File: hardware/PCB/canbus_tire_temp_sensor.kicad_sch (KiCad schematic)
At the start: 45 parts, among them J2 TC2030, J3 Conn_01x06_Male, SW1 SW_Push, SW2 SW_DPDT_x2, U1 NCV8114ASN330T1G, U2 STM32G473CB, U3 TCAN3403DRQ1, Y1 16 MHz

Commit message: Initial Schematic
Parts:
- removed C11: 0.1uF, Capacitor_SMD:C_0603_1608Metric, symbol Device:C_Small
- removed C12, C13: 1uF, Capacitor_SMD:C_0603_1608Metric, symbol Device:C_Small
- removed C16: 4.7nF, Capacitor_SMD:C_0603_1608Metric, symbol Device:C_Small
- removed D4: LED, LED_SMD:LED_0603_1608Metric, symbol Device:LED
- removed H1, H2, H3, H4: MountingHole_Pad, MountingHole:MountingHole_3.2mm_M3_ISO7380_Pad_TopBottom, symbol Mechanical:MountingHole_Pad
- removed J3: Conn_01x06_Male, Connector_Molex:Molex_Micro-Fit_3.0_43650-0610_1x06-1MP_P3.00mm_Horizontal, symbol Connector:Conn_01x06_Male
- removed JP2: SolderJumper_2_Bridged, Jumper:SolderJumper-2_P1.3mm_Bridged2Bar_Pad1.0x1.5mm, symbol Jumper:SolderJumper_2_Bridged
- removed R1: 10k, Resistor_SMD:R_0603_1608Metric, symbol Device:R
- removed R10: 1k, Resistor_SMD:R_0603_1608Metric, symbol Device:R
- removed R12: 60 250mW, Resistor_SMD:R_0805_2012Metric, symbol Device:R
- removed R13: 60 250 mW, Resistor_SMD:R_0805_2012Metric, symbol Device:R
- removed R6: 22, Resistor_SMD:R_0603_1608Metric, symbol Device:R
- removed SW2: SW_DPDT_x2, Button_Switch_SMD:SW_DPDT_CK_JS202011JCQN, symbol Switch:SW_DPDT_x2
- removed U1: NCV8114ASN330T1G, Package_TO_SOT_SMD:TSOT-23-5, symbol Regulator_Linear:NCV8114ASN330T1G
- removed U2: STM32G473CB, Package_QFP:LQFP-48_7x7mm_P0.5mm, symbol MCU_ST_STM32G4:STM32G473CB
- added C?: 1uF, Capacitor_SMD:C_0603_1608Metric, symbol Device:C_Small
- added C? (x2): (no value), Capacitor_SMD:C_0603_1608Metric, symbol Device:C_Small
- added C?: 0.1uF, Capacitor_SMD:C_0603_1608Metric, symbol Device:C_Small
- added D?: (no value), symbol Device:D_TVS
- added J?: (no value), symbol Connector_Generic:Conn_01x04
- added R?: (no value), symbol Device:R_Small
- added R?: 4.7k, symbol Device:R_Small
- added TP? (x6): (no value), symbol Connector:TestPoint
- added U?: (no value), symbol canbus_tire_temp_sensor:TLE42744DV33ATMA1
- added U?: (no value), symbol MCU_ST_STM32F0:STM32F042K6Ux
- added U?: (no value), symbol canbus_tire_temp_sensor:MLX90641
- C1: value 10uF -> (none)
- C10, C9: value 0.1uF -> (none)
- C3, C4: value 1uF -> (none)
- C6, C8: value 16pF -> (none)
- Y1: value 16 MHz -> (none)
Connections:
- net +3V3: now also J2.1 (Pin_1), C?.1, C?.2, R?.1, R?.1, TP?.1, U?.1 (VDD), U?.17 (VDDIO2), U?.2 (VDD), U?.3 (Q), U?.5 (VDDA)
- net BOOT0: now also JP1.2 (C), U?.31 (PF11)
- net CANH: now also J?.3 (Pin_3)
- net CANL: now also J?.4 (Pin_4)
- net GND: now also C6.1, C?.1, C?.1, C?.1, C?.2, D?.2 (A2), J?.2 (Pin_2), TP?.1, U?.2 (GND), U?.3 (GND), U?.33 (VSS); no longer C6.2
- net NRST: now also U?.4 (NRST)
- net OSC_IN: now also C6.2, U?.2 (PF0); no longer C6.1
- net OSC_OUT: now also U?.3 (PF1)
- net SWCLK: now also U?.24 (PA14)
- net SWDIO: now also U?.23 (PA13)
- net CAN2_RX renamed CAN_RX
- net CAN_RX: now also TP?.1, U?.21 (PA11)
- net CAN2_STANDBY renamed CAN_STANDBY
- net CAN_STANDBY: now also U?.18 (PA8)
- net CAN2_TX renamed CAN_TX
- net CAN_TX: now also TP?.1, U?.22 (PA12)
- new net LED_STATUS_1: U?.26 (PB3)
- new net LED_STATUS_2: U?.25 (PA15)
- new net SCL: R?.2, TP?.1, U?.19 (PA9), U?.4 (SCL)
- new net SDA: R?.2, TP?.1, U?.1 (SDA), U?.20 (PA10)
- new net VCC: C?.2, C?.2, D?.1 (A1), J?.1 (Pin_1), U?.1 (I)
- no-connect marks 25 -> 0
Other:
- note added: "3.3V Regulator 400mA max, 4.5-40V input - reverse-polarity protection - over temperature protection - over current protection - short circuit protection"
- note added: "Hardware Requirements - MLX90641ESF-BCA-000-SP IR Sensor Array - I2C bus interface - non-isolated can transciever - robust, unable to break device easilly from power / CAN pins - must be powered from 5 - 12V, survive high transients"
- note added: "Molex-Microfit 3.0 Mating Plug: 0430250400 Mating Plug Terminals: 0430300001"
- note removed: "3.3V Regulator 300mA max"
- note removed: "External Bus Protection"
- note removed: "Hardware Requirements - MLX90641ESF-BCA-000-SP IR Sensor Array - I2C bus interface - non-isolated can transciever - selectable termination within device - robust, unable to break device easilly from power / CAN pins - must be powered from 12V vehicle battery"
- note removed: "Molex Micro-Fit with Pass-through"
- moved on the sheet: C14, C15, C6, C8, D1, D3, D7, D8, R11, R7, R9, U3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

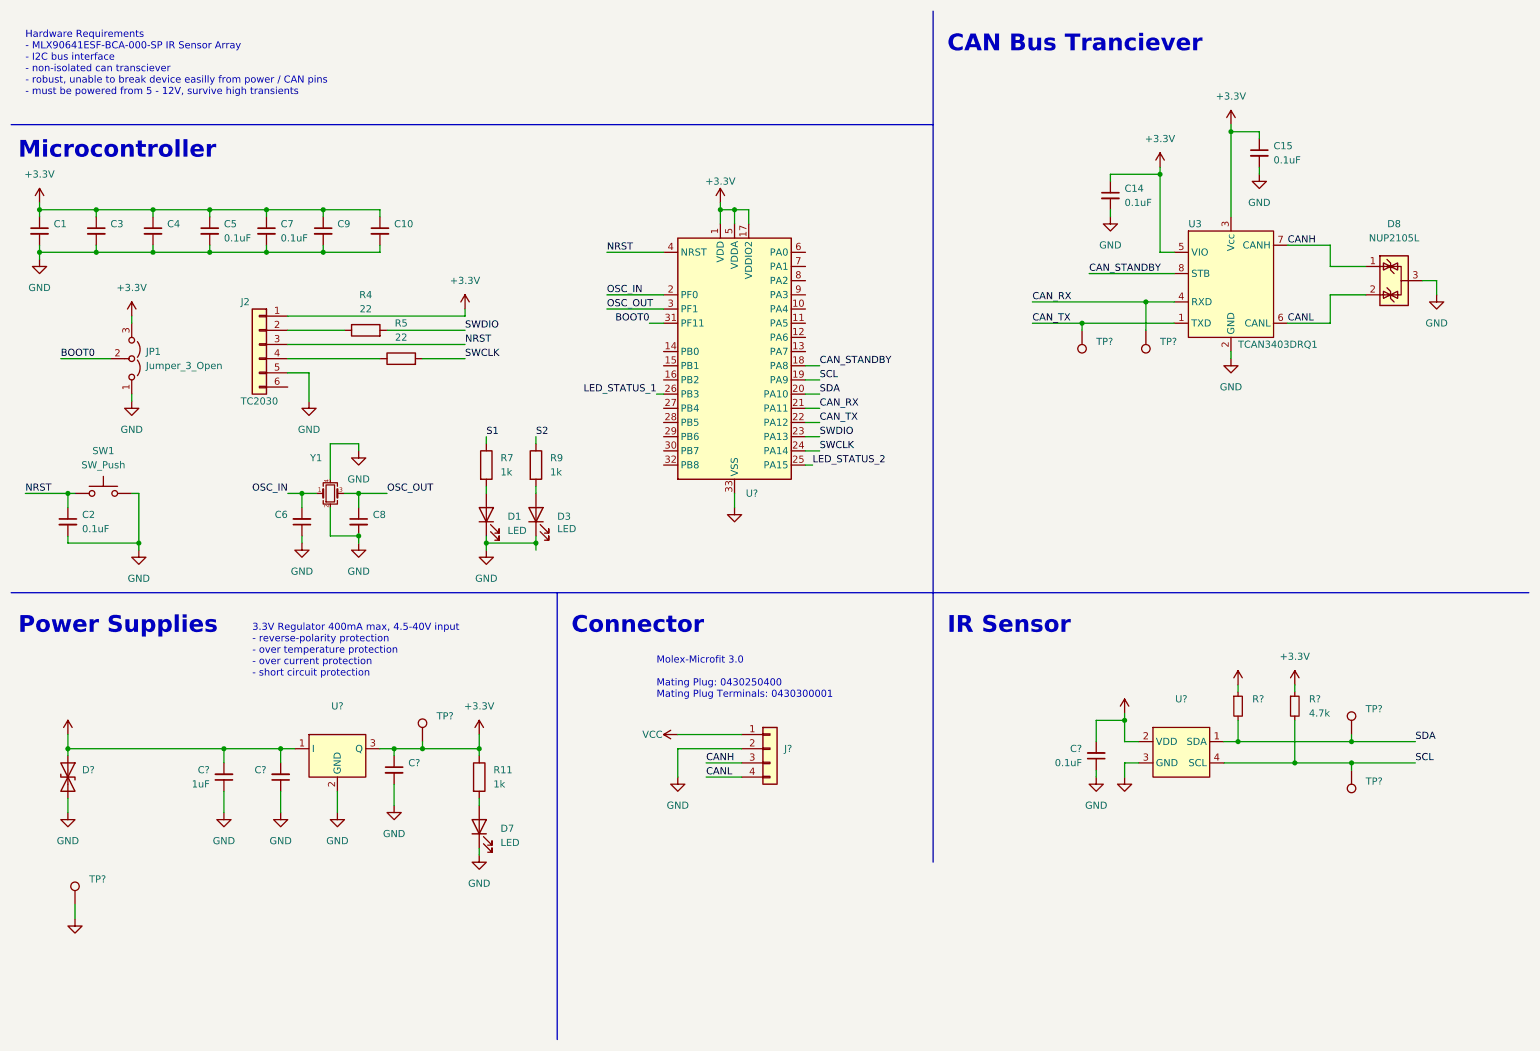
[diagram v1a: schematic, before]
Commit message: Updated footprints and ref designators
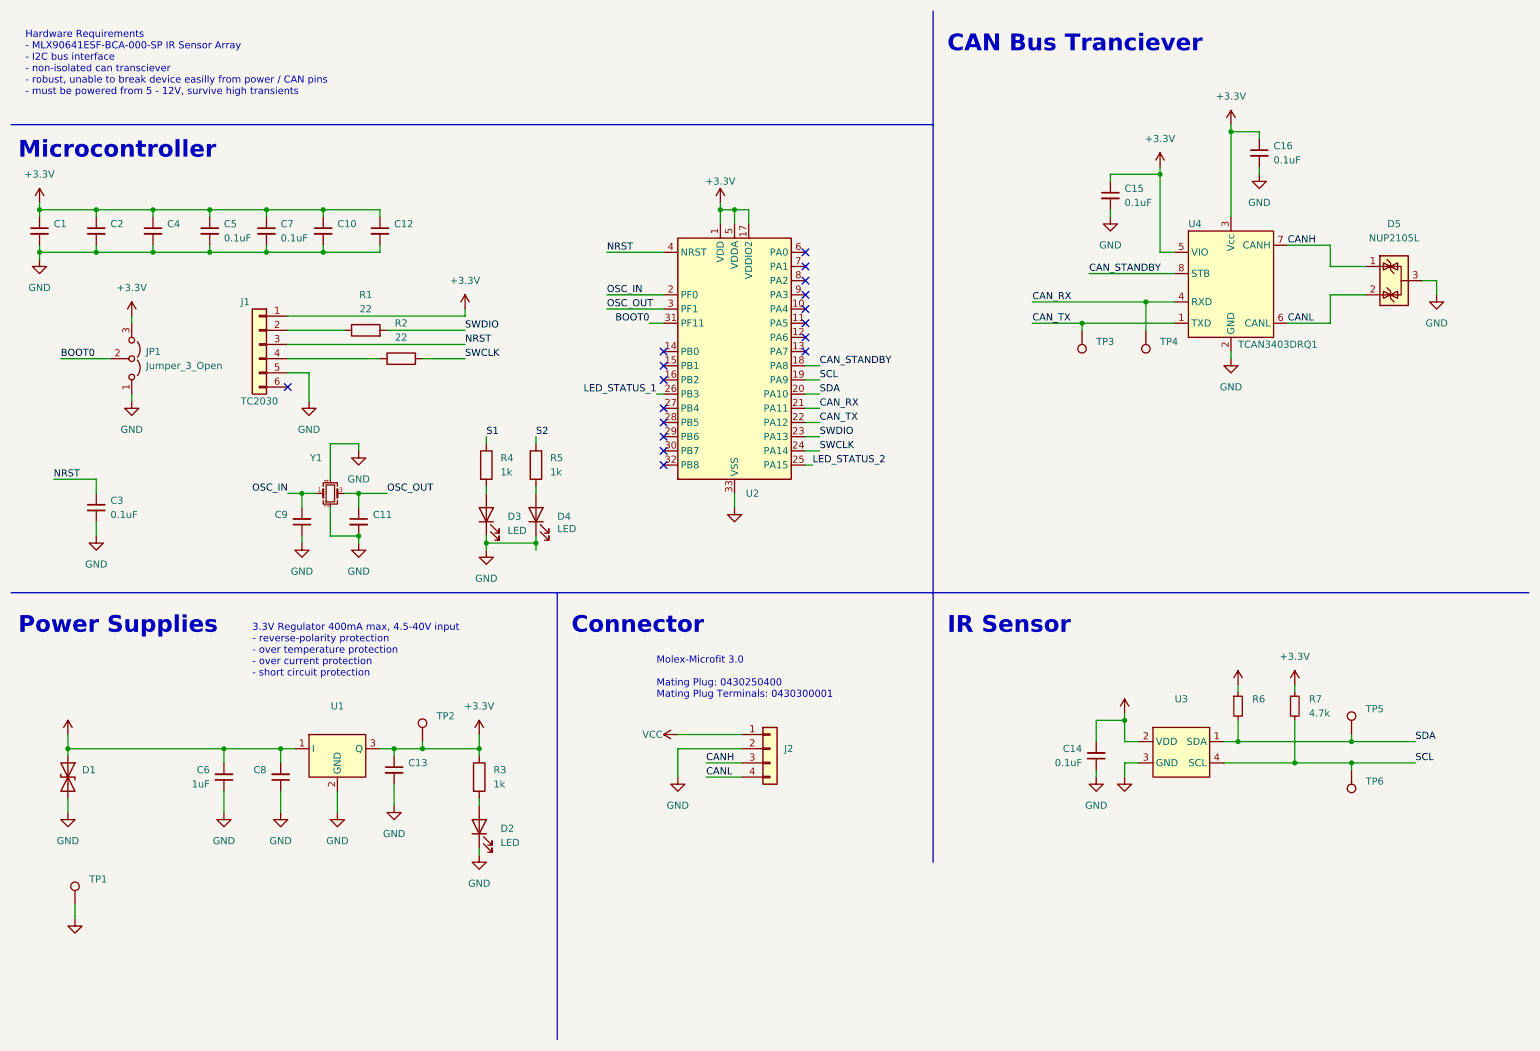
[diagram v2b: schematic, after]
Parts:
- removed SW1: SW_Push, Button_Switch_SMD:SW_SPST_B3U-1100P, symbol Switch:SW_Push
- C1: footprint Capacitor_SMD:C_0805_2012Metric -> (none)
- C13: renamed from C?; footprint Capacitor_SMD:C_0603_1608Metric -> (none)
- JP1: footprint Connector_PinHeader_2.54mm:PinHeader_1x03_P2.54mm_Vertical -> (none)
- gave numbers to parts that had none: 16
- renumbered C9 to C10, C8 to C11, C10 to C12, C14 to C15, C15 to C16, C3 to C2, C2 to C3, C6 to C9, D7 to D2, D1 to D3, D3 to D4, D8 to D5, J2 to J1, R4 to R1, R5 to R2, R11 to R3, R7 to R4, R9 to R5, U3 to U4
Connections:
- no-connect marks 0 -> 17
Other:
- moved on the sheet: C3

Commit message: initial component placement
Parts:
- J1: footprint Connector:Tag-Connect_TC2030-IDC-FP_2x03_P1.27mm_Vertical -> (none)
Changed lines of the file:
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@@
     (property "Reference" "J1" (id 0) (at 54.61 64.77 0))
     (property "Value" "TC2030" (id 1) (at 57.15 82.55 0))
-    (property "Footprint" "Connector:Tag-Connect_TC2030-IDC-FP_2x03_P1.27mm_Vertical" (id 2) (at 57.15 72.39 0)
+    (property "Footprint" "" (id 2) (at 57.15 72.39 0)
       (effects (font (size 1.27 1.27)) hide)
     )
@@
     )
     (path "/e1695a73-b49f-4d61-a6b4-7f4c0deb5b95"
-      (reference "J1") (unit 1) (value "TC2030") (footprint "Connector:Tag-Connect_TC2030-IDC-FP_2x03_P1.27mm_Vertical")
+      (reference "J1") (unit 1) (value "TC2030") (footprint "Connector:Tag-Connect_TC2030-IDC-NL_2x03_P1.27mm_Vertical")
     )
     (path "/e50c8539-9931-4edc-af04-1179e90eaec9"

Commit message: Initial board layout
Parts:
- C1: value (none) -> 4.7uF; footprint (none) -> Capacitor_SMD:C_0603_1608Metric
- C10: value (none) -> 10nF
- C11, C9: value (none) -> 12pF
- C12: value (none) -> 1uF
- C13: value (none) -> 22uF; footprint (none) -> Capacitor_SMD:C_0805_2012Metric
- C2: value (none) -> 4.7uF
- C4, C8: value (none) -> 0.1uF
- D1: value (none) -> SMBJ36CA-13-F; footprint (none) -> Diode_SMD:D_SMB
- J1: footprint (none) -> Connector:Tag-Connect_TC2030-IDC-NL_2x03_P1.27mm_Vertical
- J2: value (none) -> 0430450423; footprint (none) -> Connector_Molex:Molex_Micro-Fit_3.0_43045-0421_2x02-1MP_P3.00mm_Horizontal
- JP1: footprint (none) -> Jumper:SolderJumper-3_P1.3mm_Open_RoundedPad1.0x1.5mm
- R6: value (none) -> 4.7k; footprint (none) -> Resistor_SMD:R_0603_1608Metric
- R7: footprint (none) -> Resistor_SMD:R_0603_1608Metric
- TP1: value (none) -> GND; footprint (none) -> TestPoint:TestPoint_Pad_D2.0mm
- TP2: value (none) -> 3.3V; footprint (none) -> TestPoint:TestPoint_Pad_D2.0mm
- TP3: value (none) -> CAN_TX; footprint (none) -> TestPoint:TestPoint_Pad_D1.0mm
- TP4: value (none) -> CAN_RX; footprint (none) -> TestPoint:TestPoint_Pad_D1.0mm
- TP5: value (none) -> SDA; footprint (none) -> TestPoint:TestPoint_Pad_D1.0mm
- TP6: value (none) -> SCL; footprint (none) -> TestPoint:TestPoint_Pad_D1.0mm
- U1: value (none) -> TLE42744DV33ATMA1; footprint (none) -> Package_TO_SOT_SMD:TO-252-3_TabPin2
- U2: value (none) -> STM32F042K6Ux; footprint (none) -> Package_DFN_QFN:QFN-32-1EP_5x5mm_P0.5mm_EP3.45x3.45mm
- U3: value (none) -> MLX90641ESF-BCA-000-SP; footprint (none) -> Package_TO_SOT_THT:TO-39-4_Window
- Y1: value (none) -> ECS-160-10-36Q-AES-TR
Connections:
- net S1 is gone; now on net LED_STATUS_1: R4.1
- net S2 is gone; now on net LED_STATUS_2: R5.1
- net CANH renamed CAN_P
- net CANL renamed CAN_N

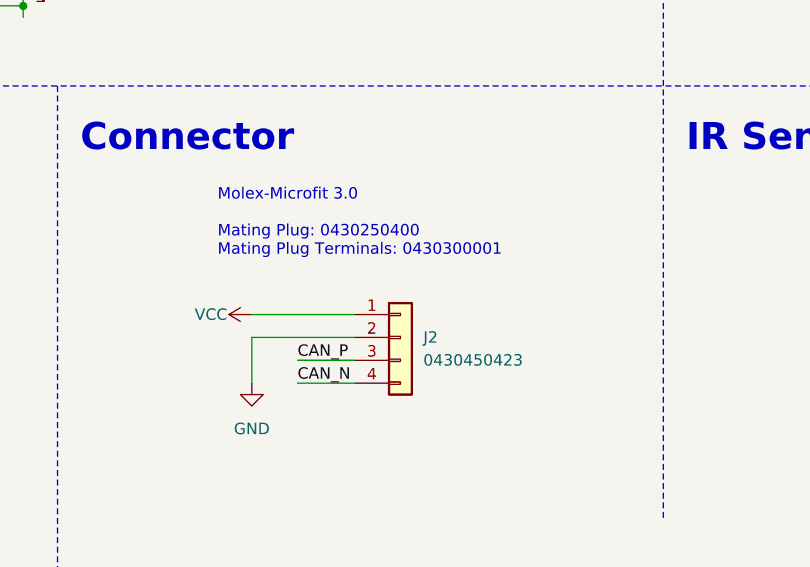
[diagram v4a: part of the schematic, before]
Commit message: Updated connector, fixed MLX footprint
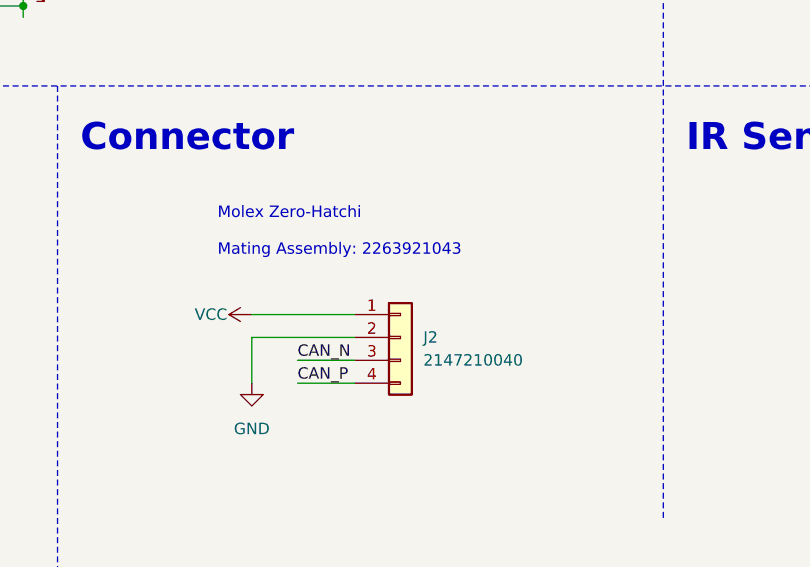
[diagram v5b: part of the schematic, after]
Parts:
- J2: value 0430450423 -> 2147210040; footprint Connector_Molex:Molex_Micro-Fit_3.0_43045-0421_2x02-1MP_P3.00mm_Horizontal -> canbus_tire_temp_sensor:Molex_Zero_Hatchi_2147210040
- U3: footprint Package_TO_SOT_THT:TO-39-4_Window -> canbus_tire_temp_sensor:MLX90641
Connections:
- net CAN_N: now also J2.3 (Pin_3); no longer J2.4 (Pin_4)
- net CAN_P: now also J2.4 (Pin_4); no longer J2.3 (Pin_3)
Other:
- note added: "Molex Zero-Hatchi Mating Assembly: 2263921043"
- note removed: "Molex-Microfit 3.0 Mating Plug: 0430250400 Mating Plug Terminals: 0430300001"
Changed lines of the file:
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@@
 		)
 	)
-	(text "Molex-Microfit 3.0\n\nMating Plug: 0430250400\nMating Plug Terminals: 0430300001"
+	(text "Molex Zero-Hatchi\n\nMating Assembly: 2263921043"
 		(exclude_from_sim no)
 		(at 128.27 135.89 0)
@@
 		)
 	)
-	(label "CAN_P"
+	(label "CAN_N"
 		(at 137.16 147.32 0)
 		(effects
@@
 		)
 	)
-	(label "CAN_N"
+	(label "CAN_P"
 		(at 137.16 149.86 0)
 		(effects
@@
 			)
 		)
-		(property "Footprint" "Package_TO_SOT_THT:TO-39-4_Window"
+		(property "Footprint" "canbus_tire_temp_sensor:MLX90641"
 			(at 228.6 146.05 0)
 			(effects
@@
 			)
 		)
-		(property "Value" "0430450423"
+		(property "Value" "2147210040"
 			(at 151.13 147.3199 0)
 			(effects
@@
 			)
 		)
-		(property "Footprint" "Connector_Molex:Molex_Micro-Fit_3.0_43045-0421_2x02-1MP_P3.00mm_Horizontal"
+		(property "Footprint" "canbus_tire_temp_sensor:Molex_Zero_Hatchi_2147210040"
 			(at 148.59 144.78 0)
 			(effects
